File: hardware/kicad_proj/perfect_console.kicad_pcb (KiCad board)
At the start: 2 copper layers, 70 x 95 mm, 68 parts, among them J1 R_Out, J10 PWR_OUT_Pins, J11 GPIO5-7, J12 USB_Out, J13 I2C, J14 ESP_UART, J15 CH_Flash, J16 CH_UART, J17 Micro_SD_Card, J18 GPIO41, J2 Jack_3.5, J3 L_Out, J4 USB, J5 TP4056_WO_Protect, J6 Bat, J7 PWR_Btn, J8 BTN_Pins, J9 PTT_Btn, Q1 NMOS, Q2 NMOS, Q3 NMOS, Q4 NMOS, Q5 NMOS, Q6 NMOS, SW1 Reset, SW2 Boot, U1 ESP32-S3-WROOM, U2 Display, U3 PCM5102, U4 PAM8403, U5 CH32V006E8R6, U6 USBLC6-2SC6, U7 DC-DC, U8 LoRa, U9 Mic

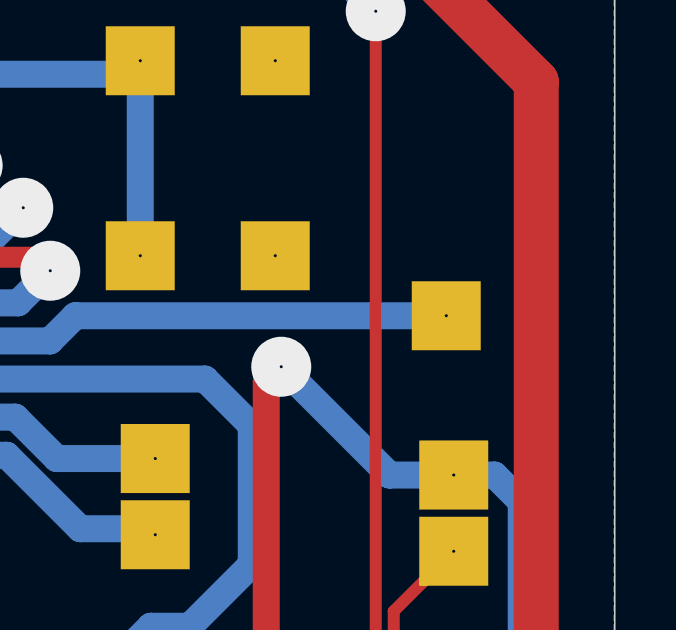
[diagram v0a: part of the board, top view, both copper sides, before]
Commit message: Виправлено позицію піна на платі
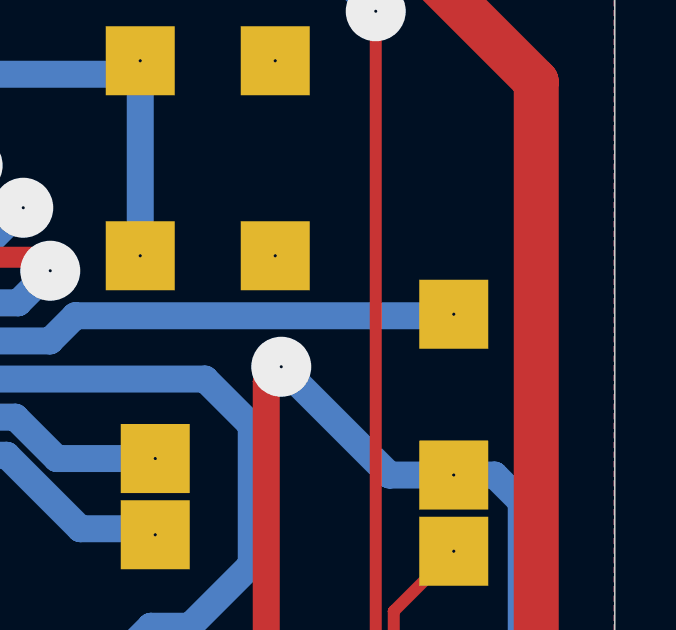
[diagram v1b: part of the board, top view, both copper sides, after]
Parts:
- moved J18 0.25 mm to (330.1, 192.2)
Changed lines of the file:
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@@
 		(tags "capacitor")
 		(property "Reference" "C5"
-			(at 0 -1.85 360)
+			(at 0 -1.85 0)
 			(layer "F.SilkS")
 			(hide yes)
@@
 		)
 		(property "Value" "1uF"
-			(at 0 0 360)
+			(at 0 0 0)
 			(layer "F.Fab")
 			(effects
@@
 		)
 		(fp_text user "${REFERENCE}"
-			(at 0 0 360)
+			(at 0 0 0)
 			(layer "F.Fab")
 			(hide yes)
@@
 		(tags "capacitor")
 		(property "Reference" "C2"
-			(at 0 -1.85 360)
+			(at 0 -1.85 0)
 			(layer "F.SilkS")
 			(hide yes)
@@
 		)
 		(property "Value" "0.1uF"
-			(at 0 0 360)
+			(at 0 0 0)
 			(layer "F.Fab")
 			(effects
@@
 		)
 		(fp_text user "${REFERENCE}"
-			(at 0 0 360)
+			(at 0 0 0)
 			(layer "F.Fab")
 			(hide yes)
@@
 		(tags "Through hole pin header THT 2x02 2.54mm double row")
 		(property "Reference" "U7"
-			(at -2.425 -1.275 360)
+			(at -2.425 -1.275 0)
 			(layer "B.SilkS")
 			(hide yes)
@@
 		(tags "Through hole pin header THT 1x02 2.54mm single row")
 		(property "Reference" "J16"
-			(at -2.2 -1.2 360)
+			(at -2.2 -1.2 0)
 			(layer "B.SilkS")
 			(hide yes)
@@
 		(tags "Through hole pin header THT 1x02 2.54mm single row")
 		(property "Reference" "J15"
-			(at -2.05 -1.5 360)
+			(at -2.05 -1.5 0)
 			(layer "B.SilkS")
 			(hide yes)
@@
 		)
 		(property "Value" "PAM8403"
-			(at 8.6 -8.9 -0)
+			(at 8.6 -8.9 0)
 			(unlocked yes)
 			(layer "B.SilkS")
@@
 	(footprint "Connector_PinHeader_2.54mm:PinHeader_1x01_P2.54mm_Vertical"
 		(layer "B.Cu")
-		(at 329.9 192.2 180)
+		(at 330.15 192.15 180)
 		(descr "Through hole straight pin header, 1x01, 2.54mm pitch, single row")
 		(tags "Through hole pin header THT 1x01 2.54mm single row")
@@
 		)
 		(property "Value" "GPIO41"
-			(at 0.1 2.4 -0)
+			(at 0.1 2.4 0)
 			(layer "B.SilkS")
 			(effects

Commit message: Допрацювання плати
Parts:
- added C12: 10uF, Capacitor_SMD:C_1206_3216Metric, F.Cu at (282.4, 202.6)
- added C13: 10uF, Capacitor_SMD:C_1206_3216Metric, F.Cu at (279.9, 202.6)
- added C14: 0.1uF, Capacitor_SMD:C_1206_3216Metric, F.Cu at (277.4, 202.6)
- added C15: 10uF, Capacitor_SMD:C_1206_3216Metric, F.Cu at (320.0, 176.4)
- added C16: 10uF, Capacitor_SMD:C_1206_3216Metric, F.Cu at (317.2, 176.4)
- U1: value ESP32-S3-WROOM -> ESP32-S3-WROOM1
- moved J11 2.02 mm to (285.4, 216.1)
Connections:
- net PIN_GND renamed GND
- C1 pad 1: 3V3 -> +3V3
- C10 pad 1: 3V3 -> +3V3
- C11 pad 2: 3V3 -> +3V3
- C3 pad 1: 4V2 -> +4V2
- C5 pad 1: 3V3 -> +3V3
- C7 pad 1: 3V3 -> +3V3
- C8 pad 2: 3V3 -> +3V3
- C9 pad 1: 3V3 -> +3V3
- J10 pad 2: 4V2 -> +4V2
- J10 pad 3: 3V3 -> +3V3
- J17 pad 4: 3V3 -> +3V3
- J5 pad 3: 4V2 -> +4V2
- J6 pad 1: 4V2 -> +4V2
- R13 pad 1: 4V2 -> +4V2
- R19 pad 1: 3V3 -> +3V3
- R20 pad 1: 3V3 -> +3V3
- R21 pad 1: 3V3 -> +3V3
- R22 pad 1: 3V3 -> +3V3
- R5 pad 1: 3V3 -> +3V3
- R7 pad 1: 3V3 -> +3V3
- R8 pad 2: 3V3 -> +3V3
- U1 pad 2: 3V3 -> +3V3
- U2 pad 2: 3V3 -> +3V3
- U3 pad 6: 3V3 -> +3V3
- U4 pad 8: 4V2 -> +4V2
- U5 pad 6: 4V2 -> +4V2
- U7 pad 1: 4V2 -> +4V2
- U7 pad 3: 3V3 -> +3V3
- U8 pad 6: 3V3 -> +4V2
- U9 pad VDD: 3V3 -> +3V3
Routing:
- net +4V2: track 0.00 -> 242.4 mm, vias 0 -> 4
- net 4V2: track 179.9 -> 0.00 mm, vias 2 -> 0
- net 3V3: track 47.7 -> 0.00 mm, vias 3 -> 0
- net +3V3: track 0.00 -> 47.7 mm, vias 0 -> 3
- net GND1: track 102.6 -> 112.7 mm
- net Net-(Q3-D): track 4.64 -> 13.1 mm
- net VVAL: track 47.5 -> 52.7 mm
- net GPIO7: track 32.3 -> 30.3 mm
- net CH_RESET: track 32.7 -> 31.1 mm
- net GPIO6: track 30.0 -> 28.7 mm
- net GPIO5: track 28.6 -> 27.7 mm
- net GND: track 194.6 -> 193.8 mm
- added copper zone on F.Cu, net +3V3
- removed copper zone on F.Cu, net 3V3

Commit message: Допрацювання схеми
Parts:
- removed the C2 at (322.3, 203.8)
- removed the R5 at (322.4, 206.9)
- added C14: 1uF, Capacitor_SMD:C_1206_3216Metric, F.Cu at (322.4, 203.8)
- added R22: 10K, Resistor_SMD:R_1206_3216Metric_Pad1.30x1.75mm_HandSolder, F.Cu at (322.4, 206.9)
- renumbered C9 to C1, C4 to C11, C5 to C12, C6 to C13, C7 to C15, C8 to C16, C1 to C2, C15 to C3, C16 to C4, C3 to C5, C12 to C6, C13 to C7, C14 to C8, C11 to C9, J18 to J15, J15 to J17, J17 to J18, R11 to R10, R12 to R11, R13 to R12, R14 to R13, R15 to R14, R16 to R15, R17 to R16, R18 to R17, R19 to R18, R20 to R19, R21 to R20, R22 to R21, R6 to R5, R7 to R6, R8 to R7, R9 to R8, R10 to R9, U8 to U6, U6 to U7, U9 to U8, U7 to U9
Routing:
- net GND: track 193.8 -> 193.2 mm

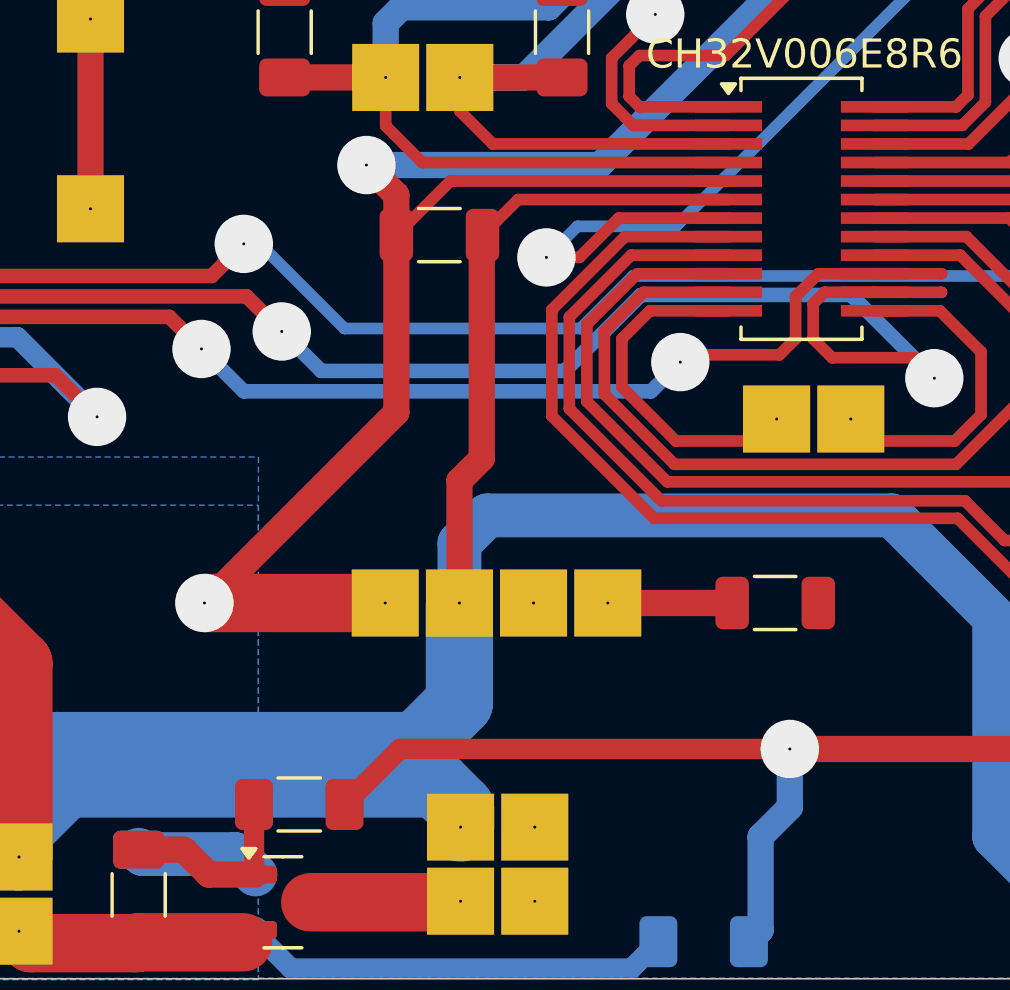
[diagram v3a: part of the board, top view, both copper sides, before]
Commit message: Покращення схеми
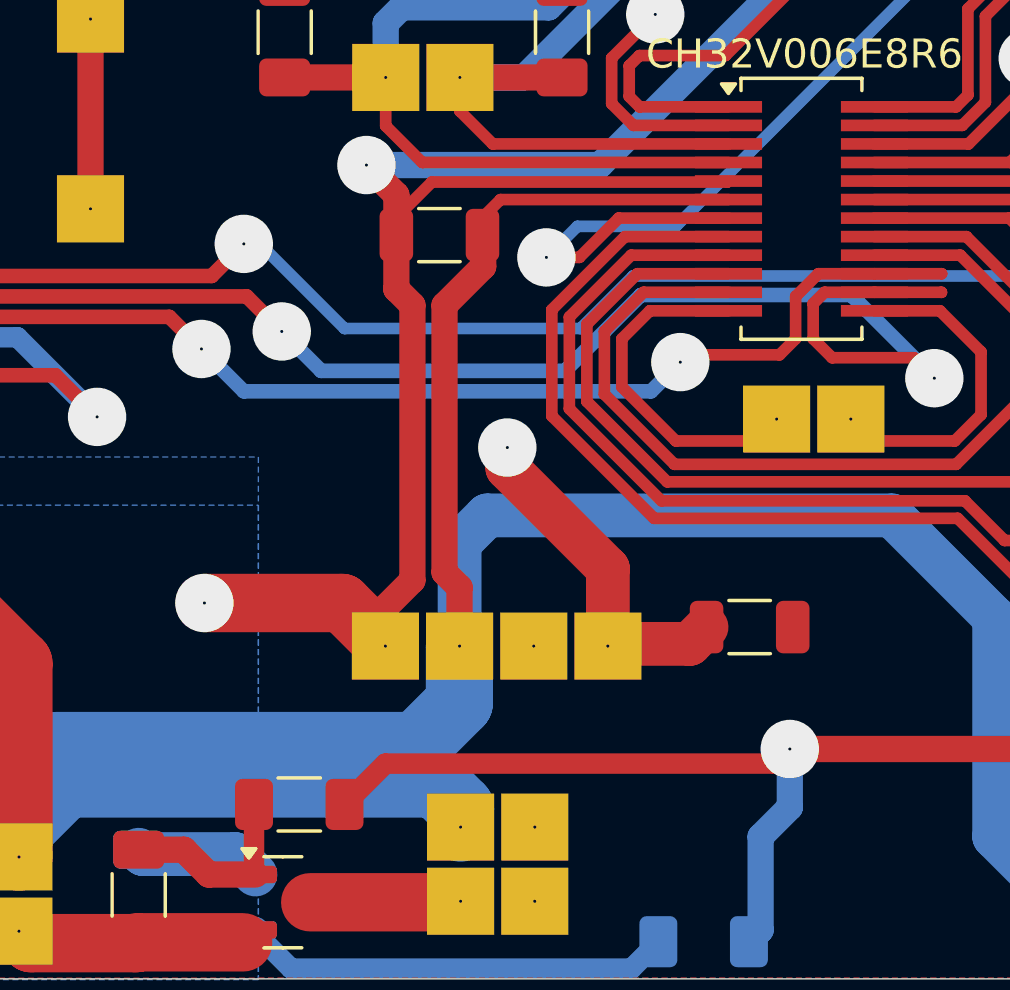
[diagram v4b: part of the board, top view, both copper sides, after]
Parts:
- C12: value 1uF -> 10uF
- moved J10 1.48 mm to (304.1, 233.9)
- moved C12 1.20 mm to (316.5, 233.2)
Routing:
- net GND1: track 113.1 -> 121.0 mm, vias 6 -> 7
- net +4V2: track 242.4 -> 244.7 mm

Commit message: Доопрацювання схеми
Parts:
- removed C14: 1uF, Capacitor_SMD:C_1206_3216Metric
- removed R22: 10K, Resistor_SMD:R_1206_3216Metric_Pad1.30x1.75mm_HandSolder
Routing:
- net GND: track 193.5 -> 176.1 mm, vias 4 -> 3
- net CH_RESET: track 31.1 -> 24.5 mm
- net PTT_BTN: track 15.8 -> 14.8 mm
- net I2C_INT: track 43.8 -> 44.4 mm
- net MIC_EN: track 112.0 -> 111.5 mm

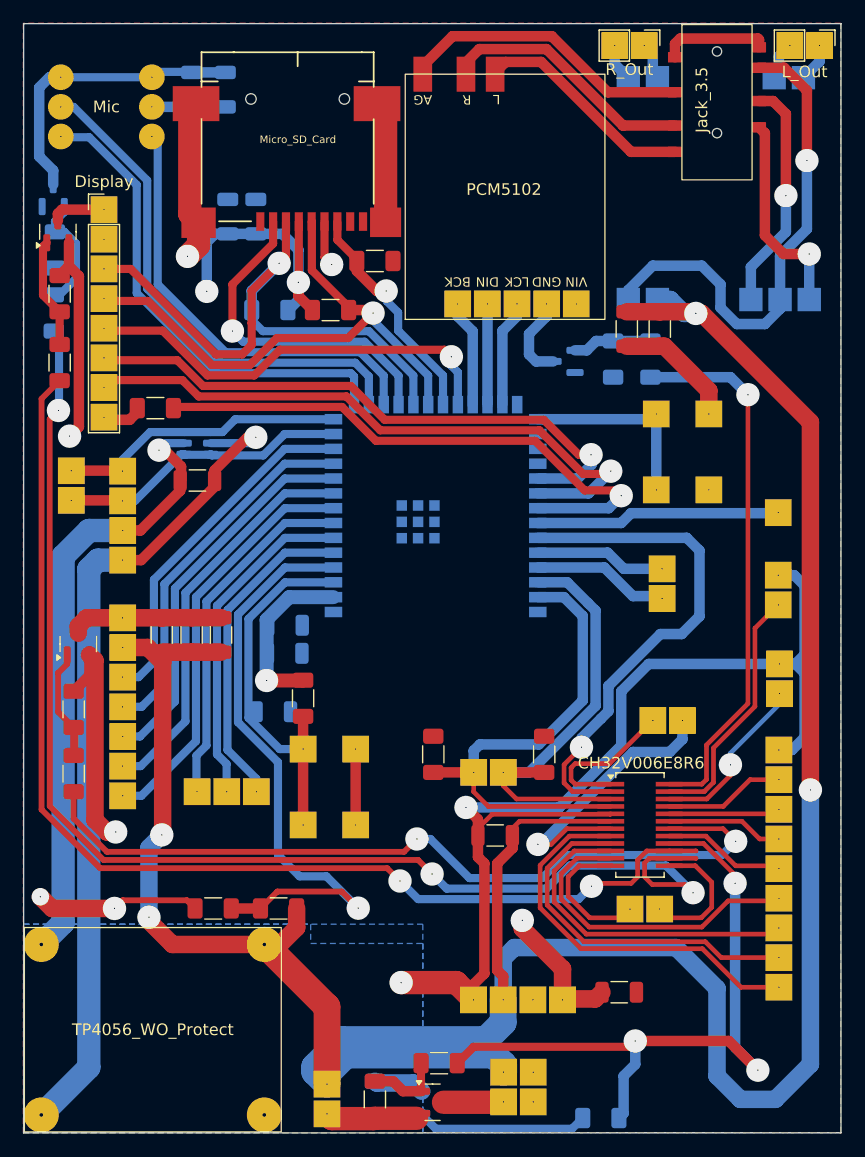
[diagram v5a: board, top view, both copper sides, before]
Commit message: Виправлення посадкових місць
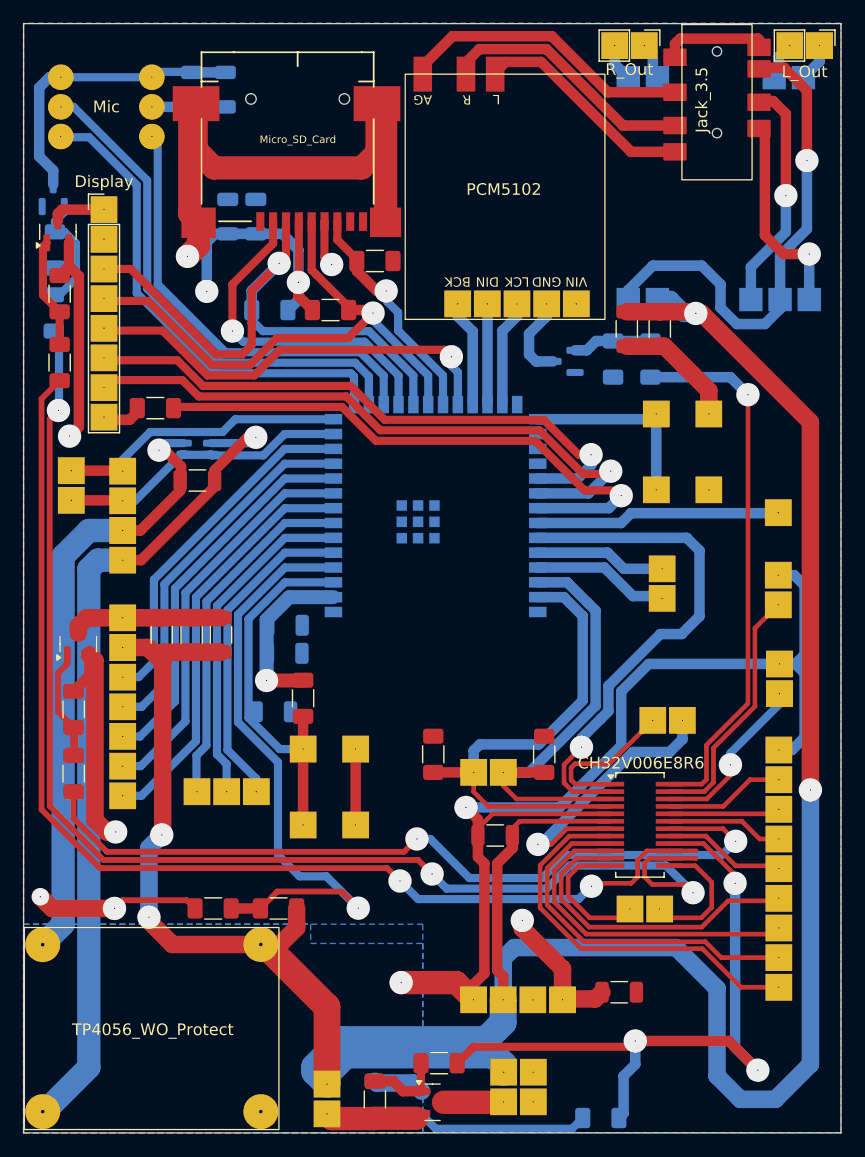
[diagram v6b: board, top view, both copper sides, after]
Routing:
- net GND1: track 121.0 -> 145.9 mm

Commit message: Корегування схеми
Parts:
- moved J2 1.67 mm to (322.2, 152.0)
- moved U4 0.73 mm to (333.8, 154.6)
- moved SW2 0.72 mm to (324.3, 190.9)
- moved J1 0.57 mm to (318.1, 152.1)
- moved R4 0.15 mm to (319.3, 179.1)
- moved R5 0.10 mm to (316.0, 179.1)
- moved J3 0.07 mm to (333.7, 152.1)
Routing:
- net Net-(J2-GN): track 43.0 -> 50.1 mm
- net Net-(J1-Pin_1): track 3.22 -> 4.19 mm
- net Net-(J1-Pin_2): track 3.23 -> 4.21 mm
- net Net-(J2-RN): track 19.9 -> 20.8 mm
- net Net-(J3-Pin_2): track 3.30 -> 4.12 mm
- net Net-(J3-Pin_1): track 3.32 -> 4.14 mm
- net GND1: track 145.9 -> 146.6 mm
- net Net-(J2-LN): track 17.8 -> 18.6 mm
- net DOWN_BTN: track 28.8 -> 29.5 mm
- net Net-(J2-M): track 9.23 -> 9.84 mm
- net BACK_BTN: track 34.0 -> 34.6 mm
- net SPK_EN: track 46.8 -> 46.2 mm

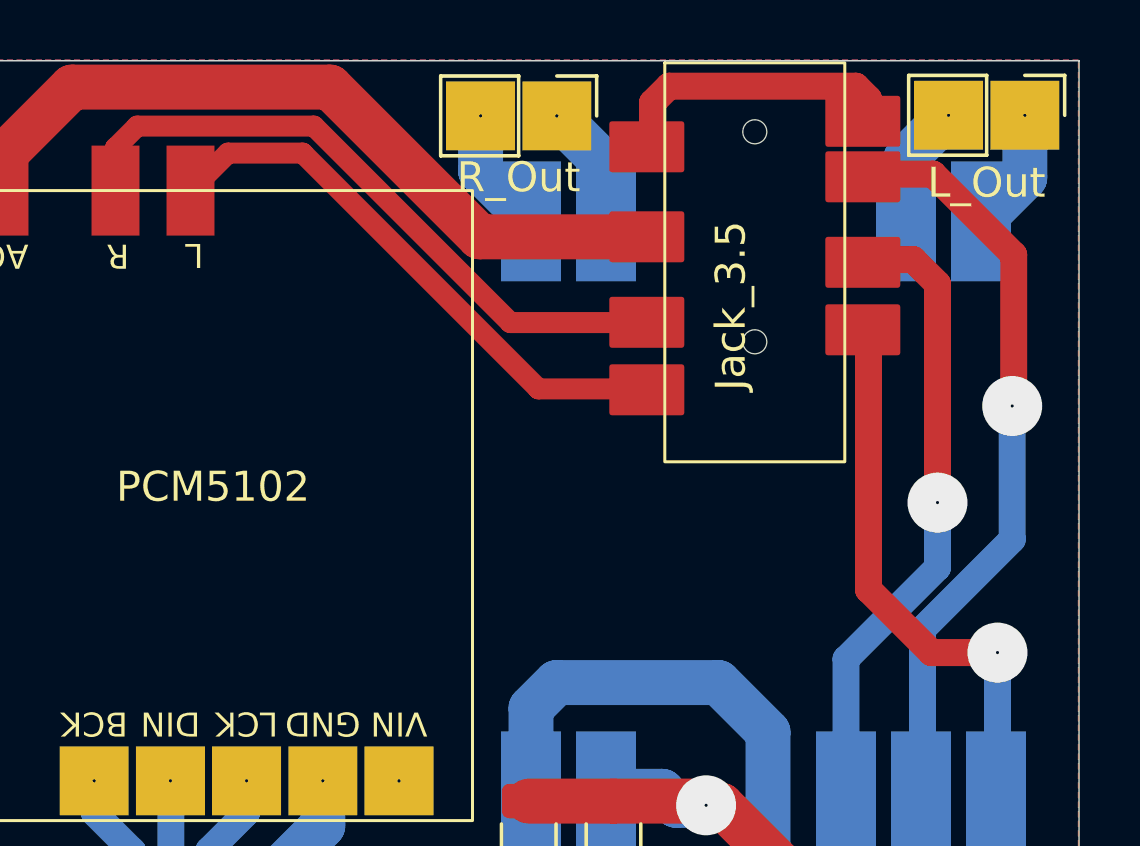
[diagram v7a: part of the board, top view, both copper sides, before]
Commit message: Виправлено символ
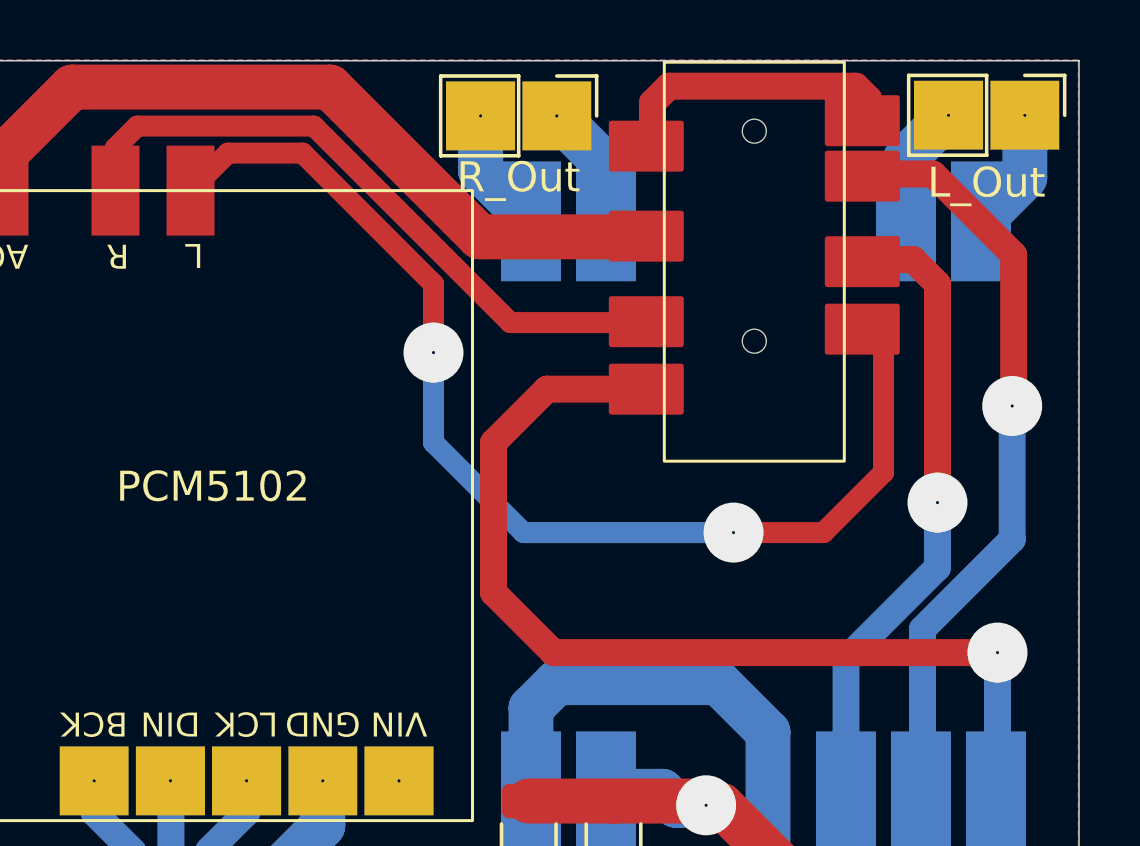
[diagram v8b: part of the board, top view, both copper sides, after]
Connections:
- U3 pad 9: Net-(J2-L) -> Net-(J2-LN)
- U4 pad 5: Net-(J2-LN) -> Net-(J2-L)
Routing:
- net Net-(J2-LN): track 18.6 -> 37.9 mm, vias 1 -> 2
- net Net-(J2-L): track 19.2 -> 33.2 mm, vias 0 -> 1
